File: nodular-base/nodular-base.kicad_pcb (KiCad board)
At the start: 4 copper layers, 83.1 x 92.5 mm, 189 parts, among them J1 Conn_02x10_Counter_Clockwise, J10 Conn_01x02_MountingPin, J11 Conn_01x08_Pin, J2 Conn_02x10_Counter_Clockwise, J3 Conn_02x10_Counter_Clockwise, J4 Conn_02x10_Counter_Clockwise, J5 Conn_02x10_Counter_Clockwise, J6 Conn_02x10_Counter_Clockwise, J7 USB_C_Receptacle_USB2.0, J8 USB_C_Receptacle_USB2.0, J9 Conn_01x30_MountingPin, SW1 SW_Push, SW2 SW_Push, SW3 SW_Push, U1 ESP32-S3-PICO-1-N8R2, U10 MT9700, U11 MT9700, U12 MT9700, U13 MT9700, U14 MT9700, U15 74LVC1G04, U16 RCLAMP0524P-ES, U17 RCLAMP0524P-ES, U18 RCLAMP0524P-ES, U19 74LVC1G04, U2 FUSB302BMPX, U20 RCLAMP0524P-ES, U21 RCLAMP0524P-ES, U22 RCLAMP0524P-ES, U23 74LVC1G04, U24 AW9523B, U25 AW9523B, U26 AW9523B, U27 RCLAMP0524P-ES, U28 RCLAMP0524P-ES, U29 RCLAMP0524P-ES, U3 BQ25895RTW, U30 RCLAMP0524P-ES, U31 74LVC1G04, U32 74LVC1G04, U33 74LVC1G04, U34 RCLAMP0524P-ES, U35 RCLAMP0524P-ES, U36 RCLAMP0524P-ES, U37 RCLAMP0524P-ES, U38 RCLAMP0524P-ES, U39 RCLAMP0524P-ES, U4 TCA9548APWR, U40 RCLAMP0524P-ES, U41 RCLAMP0524P-ES, U42 RCLAMP0524P-ES, U43 TLV62595DMQR, U44 RCLAMP0524P-ES, U45 RCLAMP0524P-ES, U46 RCLAMP0524P-ES, U47 RCLAMP0524P-ES, U48 RCLAMP0524P-ES, U49 RCLAMP0524P-ES, U5 FUSB302BMPX, U50 TS3USB221A, U51 MT9700, U6 74LVC1G17, U7 SC7A20, U8 MT9700, U9 MT9700

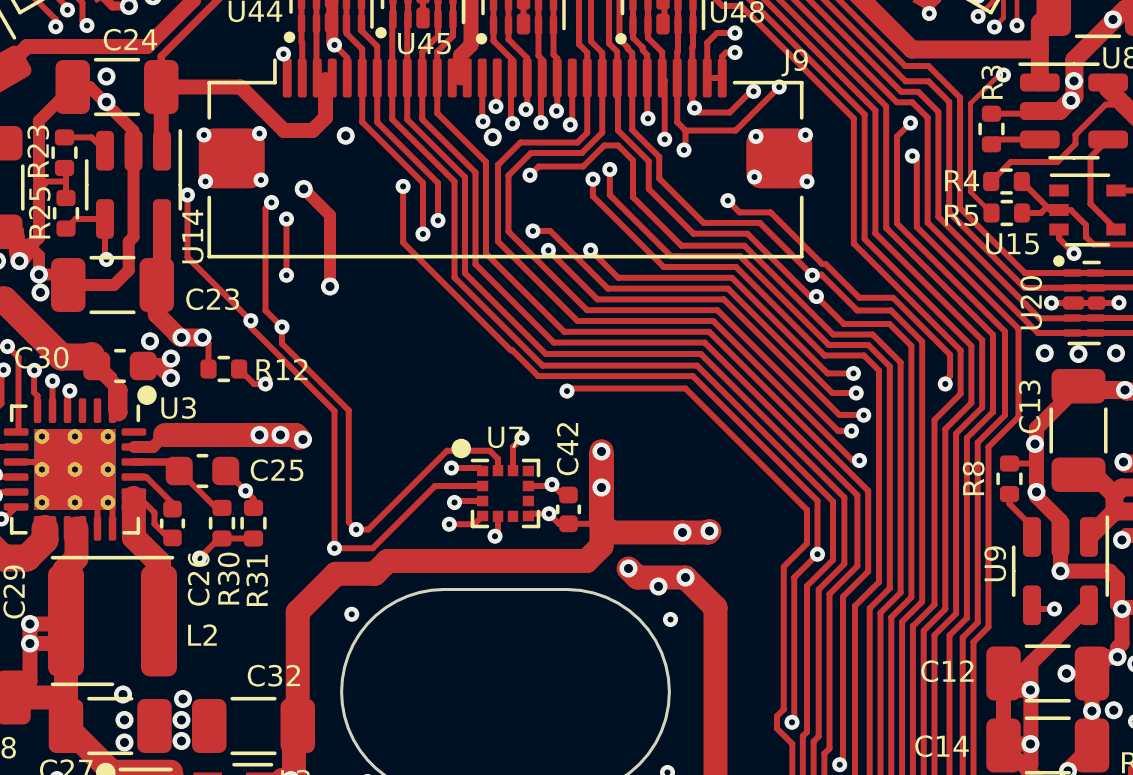
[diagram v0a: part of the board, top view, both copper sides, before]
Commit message: Add additional accelerometer-gyro option, update pin and address map, fix some ERC errors
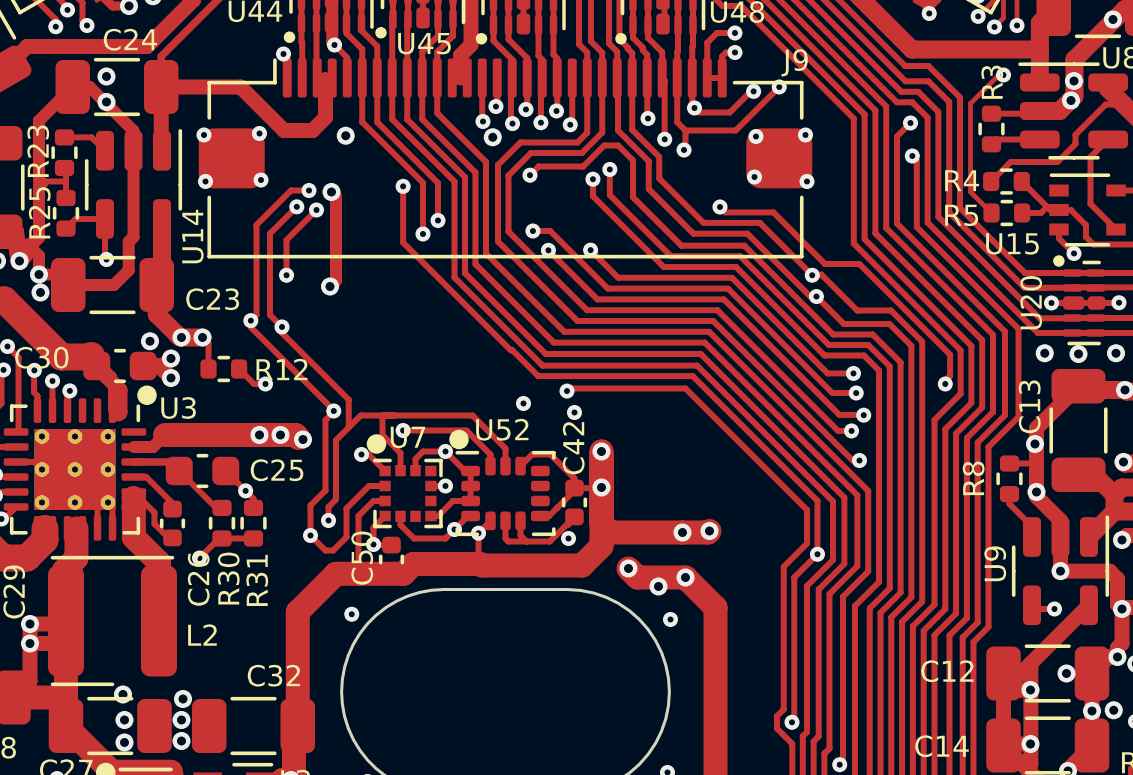
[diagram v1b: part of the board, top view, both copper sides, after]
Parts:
- added C50: 100nF, Capacitor_SMD:C_0402_1005Metric, F.Cu at (96.2, 102.2)
- added U52: LSM6DS3, Package_LGA:LGA-14_3x2.5mm_P0.5mm_LayoutBorder3x4y, F.Cu at (100.0, 100.0)
- moved U7 3.25 mm to (96.8, 100.0)
- moved C42 0.30 mm to (102.3, 100.3), turned to -90 degrees
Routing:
- net 3V3_SYS: track 506.5 -> 518.9 mm, vias 43 -> 42
- net /SDA_SYS: track 203.1 -> 212.4 mm, vias 12 -> 14
- net /INT_ACCEL: track 69.9 -> 74.0 mm
- net GND: track 368.7 -> 372.1 mm, vias 328 -> 331
- net /SCL_SYS: track 205.0 -> 208.3 mm
- net /~{INT_SYS}: track 249.9 -> 250.7 mm

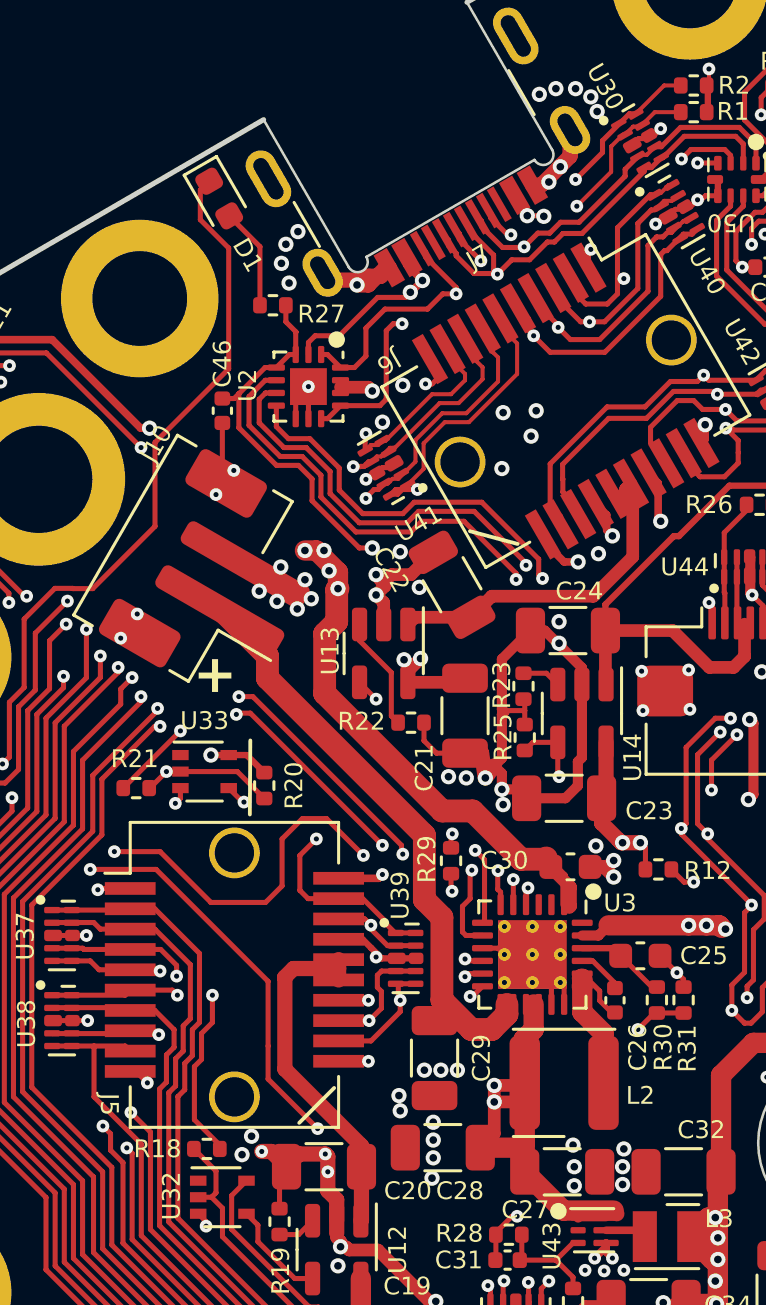
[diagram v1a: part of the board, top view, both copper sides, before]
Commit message: Implement review comments: extend zone keepout near PMIC
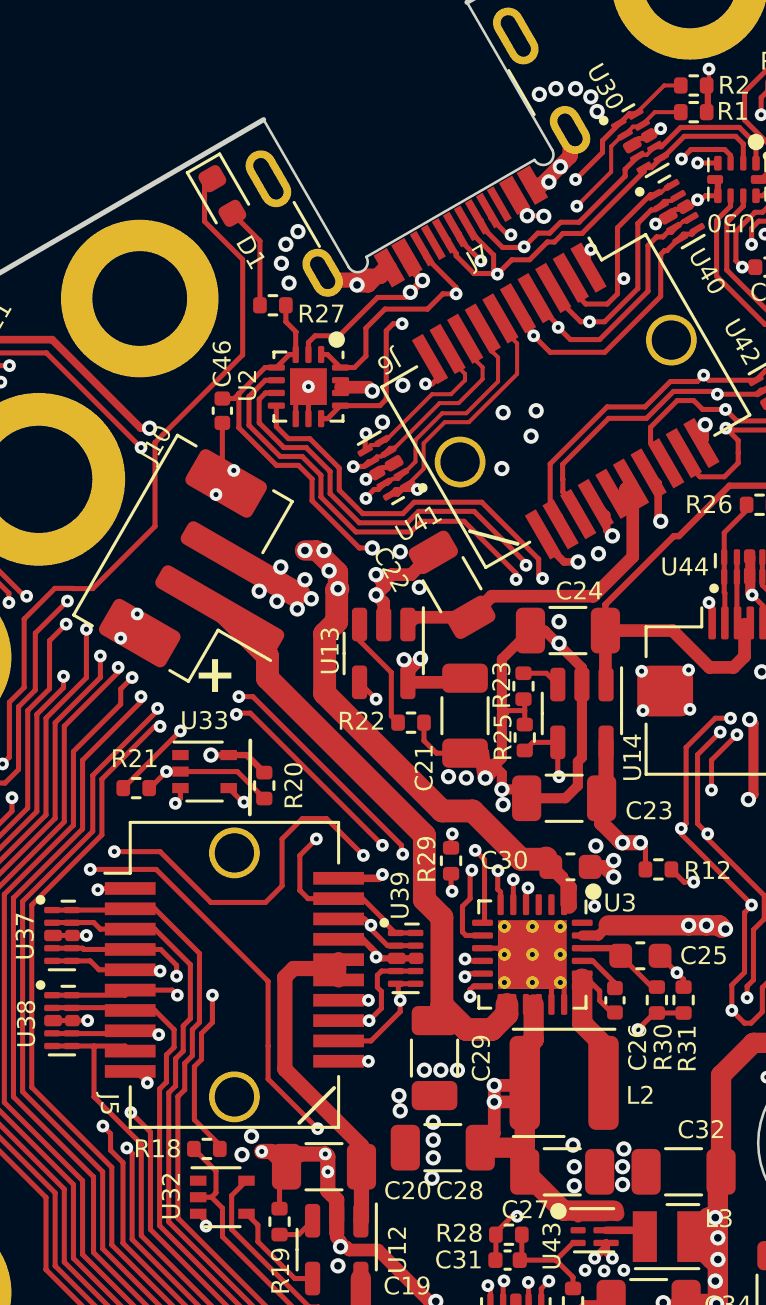
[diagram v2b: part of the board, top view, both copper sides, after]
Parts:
- moved D1 0.16 mm to (73.5, 69.3)
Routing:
- net GND: vias 331 -> 332

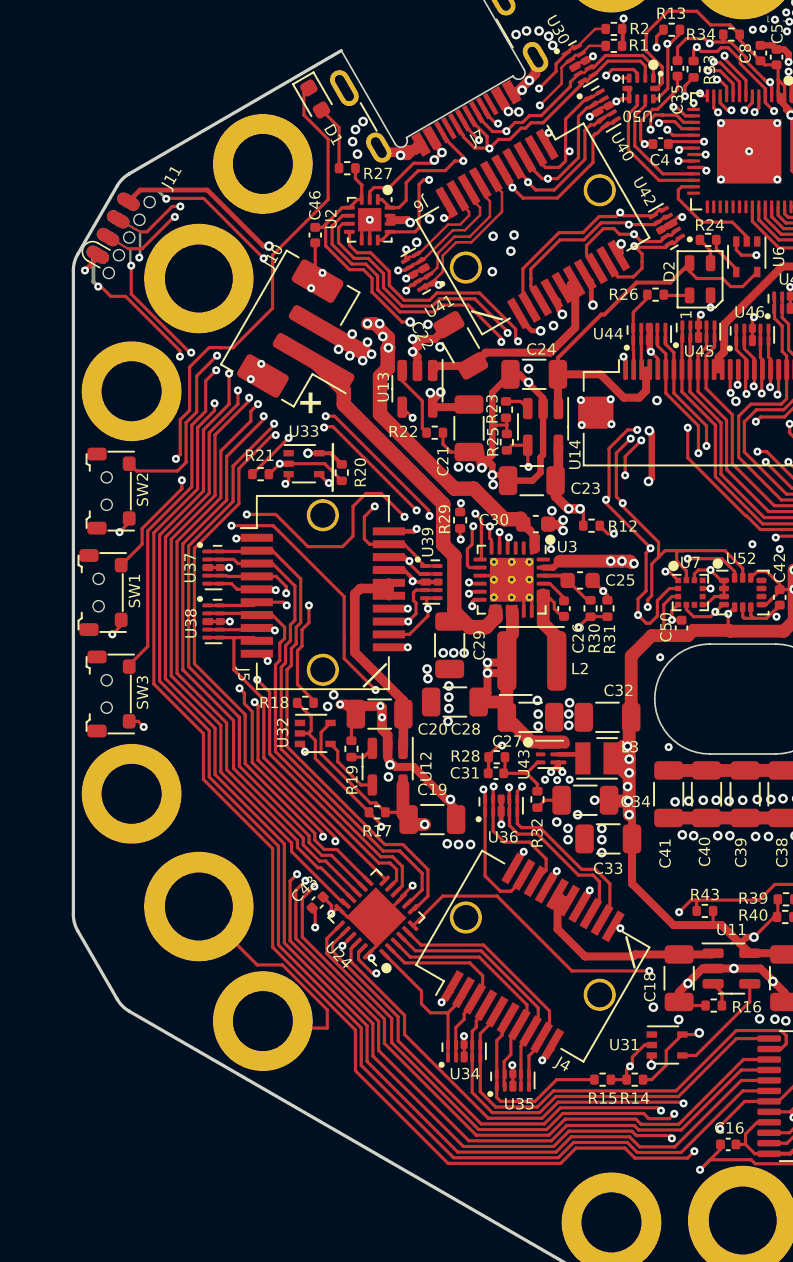
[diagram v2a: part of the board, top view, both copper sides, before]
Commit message: Optimize some via entries
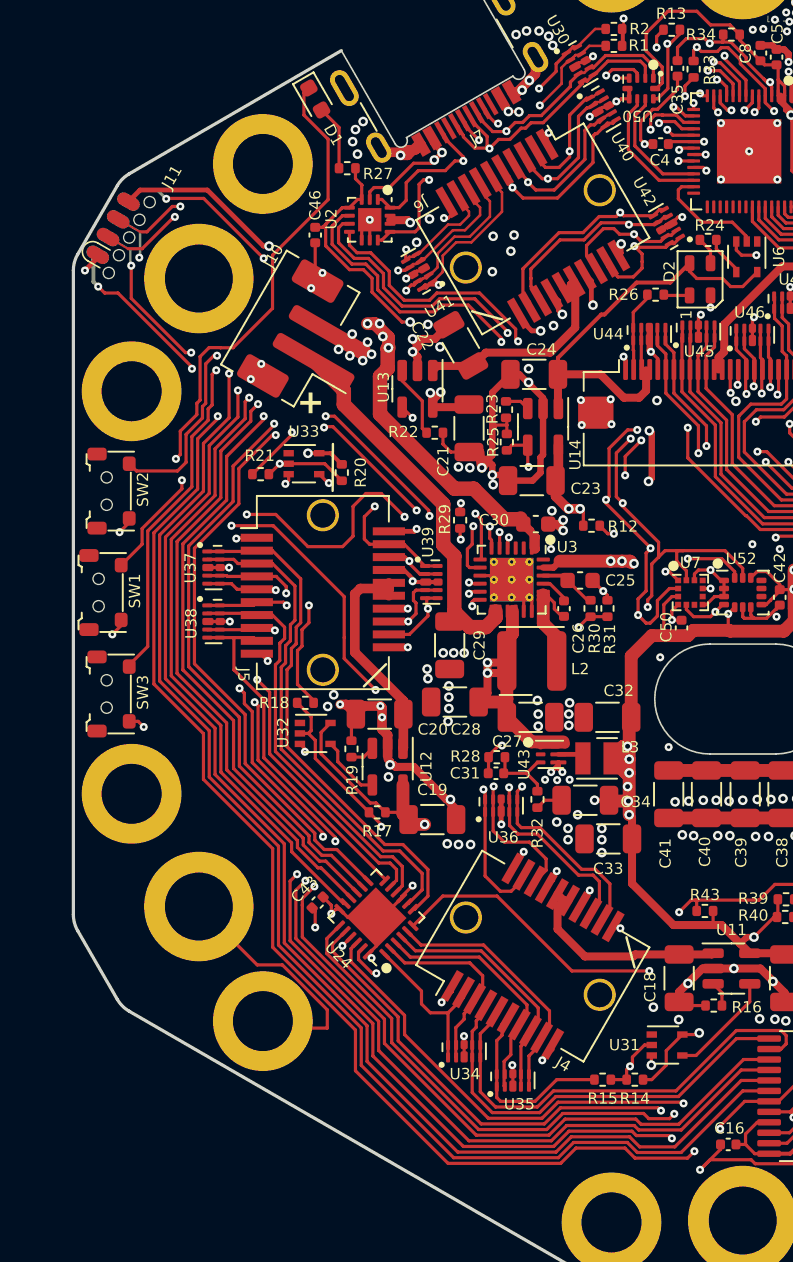
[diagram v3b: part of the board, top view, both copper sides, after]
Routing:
- net /GPIO/DET_F: track 133.4 -> 132.1 mm
